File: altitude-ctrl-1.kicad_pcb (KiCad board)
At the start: 2 copper layers, 0 parts

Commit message: pcb: import components from schem
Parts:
- added C1: 10u, Capacitor_SMD:C_0805_2012Metric, F.Cu at (71.1, 154.0)
- added C10: 22u, Capacitor_SMD:C_0805_2012Metric, F.Cu at (80.0, 157.0)
- added C11: 0u1, Capacitor_SMD:C_0402_1005Metric, F.Cu at (83.2, 180.4)
- added C12: 10u, Capacitor_SMD:C_0805_2012Metric, F.Cu at (80.0, 160.0)
- added C13: 0u1, Capacitor_SMD:C_0402_1005Metric, F.Cu at (83.2, 182.3)
- added C14: 20p, Capacitor_SMD:C_0603_1608Metric, F.Cu at (89.5, 176.7)
- added C15: 20p, Capacitor_SMD:C_0603_1608Metric, F.Cu at (89.5, 179.2)
- added C16: 0u1, Capacitor_SMD:C_0402_1005Metric, F.Cu at (83.2, 184.3)
- added C17: 0u1, Capacitor_SMD:C_0402_1005Metric, F.Cu at (83.2, 186.3)
- added C18: 0u1, Capacitor_SMD:C_0402_1005Metric, F.Cu at (86.1, 176.4)
- added C19: 0u1, Capacitor_SMD:C_0402_1005Metric, F.Cu at (86.1, 178.4)
- added C2: 1u, Capacitor_SMD:C_0402_1005Metric, F.Cu at (83.2, 176.4)
- added C20: 1u, Capacitor_SMD:C_0402_1005Metric, F.Cu at (86.1, 180.4)
- added C21: 1u, Capacitor_SMD:C_0402_1005Metric, F.Cu at (86.1, 182.3)
- added C22: 0u1, Capacitor_SMD:C_0402_1005Metric, F.Cu at (86.1, 184.3)
- added C3: 1u, Capacitor_SMD:C_0402_1005Metric, F.Cu at (83.2, 178.4)
- added C4: 10u, Capacitor_SMD:C_0805_2012Metric, F.Cu at (71.1, 157.0)
- added C5: 22u, Capacitor_SMD:C_0805_2012Metric, F.Cu at (71.1, 160.0)
- added C6: 22u, Capacitor_SMD:C_0805_2012Metric, F.Cu at (75.6, 154.0)
- added C7: 22u, Capacitor_SMD:C_0805_2012Metric, F.Cu at (75.6, 157.0)
- added C8: 22u, Capacitor_SMD:C_0805_2012Metric, F.Cu at (75.6, 160.0)
- added C9: 22u, Capacitor_SMD:C_0805_2012Metric, F.Cu at (80.0, 154.0)
- added D1: SMAJ12A, Diode_SMD:D_SMA, F.Cu at (61.6, 179.3)
- added D10: YELLOW, LED_SMD:LED_0805_2012Metric, F.Cu at (68.3, 185.1)
- added D11: H5VU10U, GLCS:Diode_DFN1006, F.Cu at (86.2, 164.8)
- added D12: H5VU10U, GLCS:Diode_DFN1006, F.Cu at (86.2, 166.8)
- added D13: H5VU10U, GLCS:Diode_DFN1006, F.Cu at (86.2, 168.8)
- added D14: H5VU10U, GLCS:Diode_DFN1006, F.Cu at (86.2, 170.8)
- added D15: H5VU10U, GLCS:Diode_DFN1006, F.Cu at (86.2, 172.8)
- added D16: H5VU10U, GLCS:Diode_DFN1006, F.Cu at (89.3, 164.8)
- added D17: H5VU10U, GLCS:Diode_DFN1006, F.Cu at (89.3, 166.8)
- added D18: H5VU10U, GLCS:Diode_DFN1006, F.Cu at (89.3, 168.8)
- added D2: SMAJ12A, Diode_SMD:D_SMA, F.Cu at (61.6, 183.8)
- added D3: GREEN, LED_SMD:LED_0805_2012Metric, F.Cu at (68.3, 179.0)
- added D4: GREEN, LED_SMD:LED_0805_2012Metric, F.Cu at (68.3, 182.0)
- added D5: H5VU10U, GLCS:Diode_DFN1006, F.Cu at (83.2, 164.8)
- added D6: H5VU10U, GLCS:Diode_DFN1006, F.Cu at (83.2, 166.8)
- added D7: H5VU10U, GLCS:Diode_DFN1006, F.Cu at (83.2, 168.8)
- added D8: H5VU10U, GLCS:Diode_DFN1006, F.Cu at (83.2, 170.8)
- added D9: H5VU10U, GLCS:Diode_DFN1006, F.Cu at (83.2, 172.8)
- added FB1: 600Ω@100M, Inductor_SMD:L_0805_2012Metric, F.Cu at (85.8, 150.4)
- added FID1: Fiducial, Fiducial:Fiducial_1mm_Mask2mm, F.Cu at (54.5, 169.8)
- added FID2: Fiducial, Fiducial:Fiducial_1mm_Mask2mm, F.Cu at (54.5, 173.4)
- added FID3: Fiducial, Fiducial:Fiducial_1mm_Mask2mm, F.Cu at (54.5, 176.9)
- added H1: MountingHole, MountingHole:ToolingHole_1.152mm, F.Cu at (88.8, 131.7)
- added H2: MountingHole, MountingHole:ToolingHole_1.152mm, F.Cu at (88.8, 134.2)
- added H3: MountingHole, MountingHole:ToolingHole_1.152mm, F.Cu at (88.8, 136.6)
- added H4: MountingHole_Pad, MountingHole:MountingHole_3.2mm_M3_Pad_Via, F.Cu at (79.5, 120.1)
- added H5: MountingHole_Pad, MountingHole:MountingHole_3.2mm_M3_Pad_Via, F.Cu at (79.5, 128.0)
- added H6: MountingHole_Pad, MountingHole:MountingHole_3.2mm_M3_Pad_Via, F.Cu at (79.5, 136.0)
- added H7: MountingHole_Pad, MountingHole:MountingHole_3.2mm_M3_Pad_Via, F.Cu at (79.5, 143.9)
- added J1: Conn_01x02, TerminalBlock_Phoenix:TerminalBlock_Phoenix_MKDS-1,5-2-5.08_1x02_P5.08mm_Horizontal, F.Cu at (39.5, 122.3)
- added J10: Conn_01x02, Connector_JST:JST_XH_B2B-XH-A_1x02_P2.50mm_Vertical, F.Cu at (51.6, 163.6)
- added J2: Conn_01x02, TerminalBlock_Phoenix:TerminalBlock_Phoenix_MKDS-1,5-2-5.08_1x02_P5.08mm_Horizontal, F.Cu at (39.5, 134.5)
- added J3: Conn_01x05, TerminalBlock_Phoenix:TerminalBlock_Phoenix_MKDS-1,5-5-5.08_1x05_P5.08mm_Horizontal, F.Cu at (51.7, 122.3)
- added J4: TC2030, Connector:Tag-Connect_TC2030-IDC-NL_2x03_P1.27mm_Vertical, F.Cu at (52.1, 182.8)
- added J5: Conn_01x04_Pin, Connector_PinHeader_2.54mm:PinHeader_1x04_P2.54mm_Vertical, F.Cu at (50.4, 170.4)
- added J6: Conn_01x02, TerminalBlock_Phoenix:TerminalBlock_Phoenix_MKDS-1,5-2-5.08_1x02_P5.08mm_Horizontal, F.Cu at (39.5, 146.6)
- added J7: Conn_01x05, TerminalBlock_Phoenix:TerminalBlock_Phoenix_MKDS-1,5-5-5.08_1x05_P5.08mm_Horizontal, F.Cu at (51.7, 134.5)
- added J8: Conn_01x05, TerminalBlock_Phoenix:TerminalBlock_Phoenix_MKDS-1,5-5-5.08_1x05_P5.08mm_Horizontal, F.Cu at (51.7, 146.6)
- added J9: Conn_01x02, Connector_JST:JST_XH_B2B-XH-A_1x02_P2.50mm_Vertical, F.Cu at (51.6, 155.8)
- added JP1: Jumper_2_Small_Bridged, Connector_PinHeader_2.54mm:PinHeader_1x02_P2.54mm_Vertical, F.Cu at (85.8, 140.9)
- added R1: 10k, Resistor_SMD:R_0402_1005Metric, F.Cu at (74.5, 176.4)
- added R10: 10k, Resistor_SMD:R_0402_1005Metric, F.Cu at (77.4, 184.4)
- added R11: 10k, Resistor_SMD:R_0402_1005Metric, F.Cu at (80.3, 176.4)
- added R12: 560, Resistor_SMD:R_0603_1608Metric, F.Cu at (89.5, 181.7)
- added R13: 5k1, Resistor_SMD:R_0402_1005Metric, F.Cu at (80.3, 178.4)
- added R14: 100, Resistor_SMD:R_0402_1005Metric, F.Cu at (80.3, 180.4)
- added R15: 120, Resistor_SMD:R_1206_3216Metric, F.Cu at (86.3, 147.4)
- added R2: 1k, Resistor_SMD:R_0402_1005Metric, F.Cu at (74.5, 178.4)
- added R3: 1k, Resistor_SMD:R_0402_1005Metric, F.Cu at (74.5, 180.4)
- added R4: 5k1, Resistor_SMD:R_0402_1005Metric, F.Cu at (74.5, 182.4)
- added R5: 5k1, Resistor_SMD:R_0402_1005Metric, F.Cu at (74.5, 184.4)
- added R6: 5k1, Resistor_SMD:R_0402_1005Metric, F.Cu at (77.4, 176.4)
- added R7: 1k, Resistor_SMD:R_0402_1005Metric, F.Cu at (77.4, 178.4)
- added R8: 5k1, Resistor_SMD:R_0402_1005Metric, F.Cu at (77.4, 180.4)
- added R9: 10k, Resistor_SMD:R_0402_1005Metric, F.Cu at (77.4, 182.4)
- added SW1: SW_Push, Button_Switch_SMD:SW_SPST_TS-1088-xR020, F.Cu at (69.5, 166.1)
- added SW2: SW_SPST, TerminalBlock_Phoenix:TerminalBlock_Phoenix_MKDS-1,5-2-5.08_1x02_P5.08mm_Horizontal, F.Cu at (39.5, 158.7)
- added SW3: SW_Push, Button_Switch_SMD:SW_SPST_TS-1088-xR020, F.Cu at (69.5, 170.6)
- added SW4: SW_SPST, TerminalBlock_Phoenix:TerminalBlock_Phoenix_MKDS-1,5-2-5.08_1x02_P5.08mm_Horizontal, F.Cu at (39.5, 170.8)
- added SW5: SW_Push, Button_Switch_SMD:SW_SPST_TS-1088-xR020, F.Cu at (69.5, 175.2)
- added TC1: Thermocouple_Block, TerminalBlock_Phoenix:TerminalBlock_Phoenix_MKDS-1,5-2-5.08_1x02_P5.08mm_Horizontal, F.Cu at (39.5, 183.0)
- added TP1: TestPoint, TestPoint:TestPoint_Pad_D2.0mm, F.Cu at (85.5, 132.5)
- added TP2: TestPoint, TestPoint:TestPoint_Pad_D2.0mm, F.Cu at (85.5, 136.6)
- added U1: HT753-1, Package_TO_SOT_SMD:SOT-89-3, F.Cu at (86.9, 127.5)
- added U2: ULN2003A, Package_SO:SOIC-16_3.9x9.9mm_P1.27mm, F.Cu at (77.3, 169.7)
- added U3: LM73100, GLCS:Texas_RPW0010A_VQFN-HR-10_2x2mm_P0.5mm, F.Cu at (85.6, 118.2)
- added U4: LM73100, GLCS:Texas_RPW0010A_VQFN-HR-10_2x2mm_P0.5mm, F.Cu at (85.6, 122.3)
- added U5: MAX6675, Package_SO:SOIC-8_3.9x4.9mm_P1.27mm, F.Cu at (61.8, 167.2)
- added U6: STM32F103C8Tx, Package_QFP:LQFP-48_7x7mm_P0.5mm, F.Cu at (63.2, 158.1)
- added U7: SN65HVD230, Package_SO:SOIC-8_3.9x4.9mm_P1.27mm, F.Cu at (61.8, 173.8)
- added Y1: 8M, Crystal:Crystal_SMD_5032-2Pin_5.0x3.2mm, F.Cu at (85.9, 155.1)

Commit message: pcb: add initial sectioning
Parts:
- moved J6 220.7 mm to (260.1, 154.0), turned to 180 degrees
- moved J7 215.5 mm to (266.3, 115.2), turned to 180 degrees
- moved TC1 205.6 mm to (243.1, 154.4), turned to 180 degrees
- moved D15 194.4 mm to (268.2, 104.4), turned to 180 degrees
- moved D13 192.4 mm to (268.2, 106.4), turned to 180 degrees
- moved D11 190.5 mm to (268.2, 108.4), turned to 180 degrees
- moved D17 190.2 mm to (268.2, 102.4), turned to 180 degrees
- moved J2 187.1 mm to (225.7, 153.0), turned to 180 degrees
- moved R14 184.9 mm to (262.2, 147.1), turned to 180 degrees
- moved J8 182.1 mm to (231.1, 115.5), turned to 180 degrees
- moved U5 181.9 mm to (242.4, 145.1), turned to 180 degrees
- moved D2 168.1 mm to (225.2, 144.8), turned to 180 degrees
- moved SW4 165.2 mm to (196.2, 118.5), turned to 90 degrees
- moved J1 164.6 mm to (201.2, 152.7), turned to 180 degrees
- moved D14 160.2 mm to (233.0, 106.6), turned to 180 degrees
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
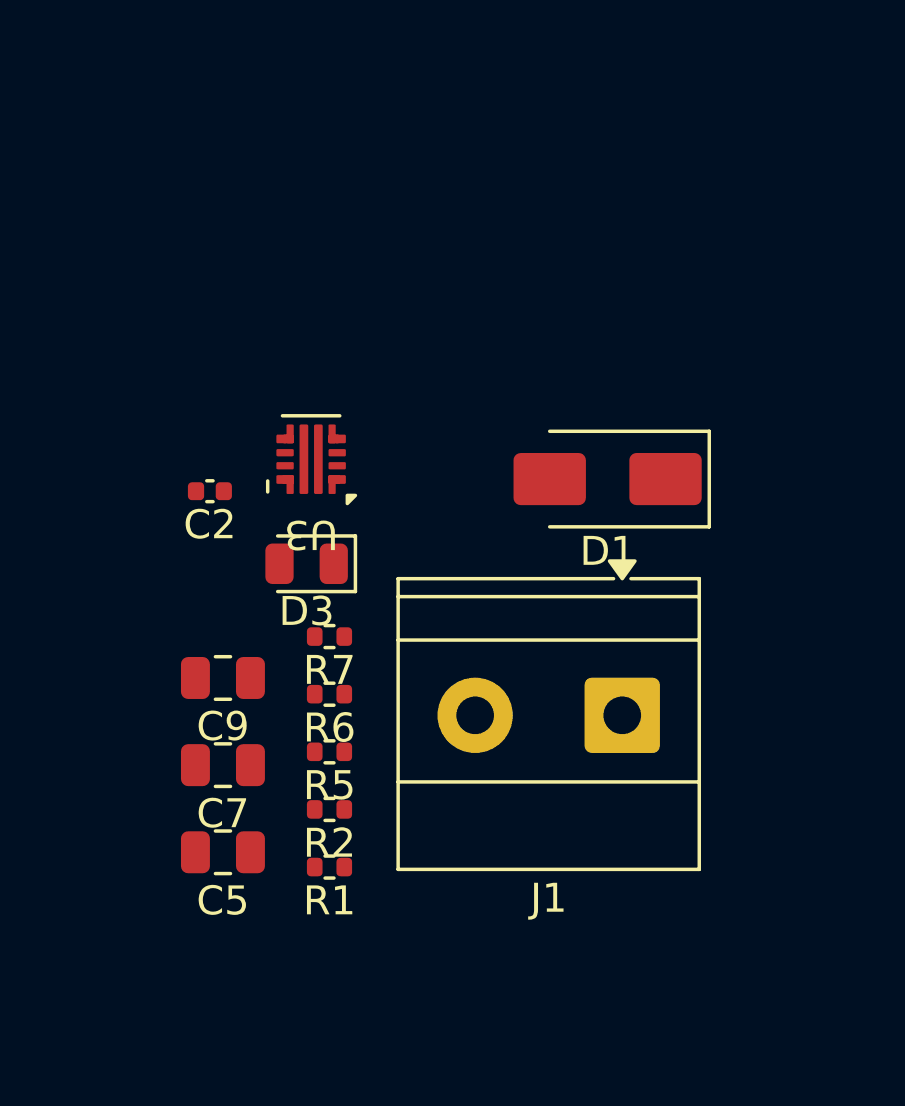
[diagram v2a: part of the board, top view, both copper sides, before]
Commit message: pcb: add +12v input protection layout
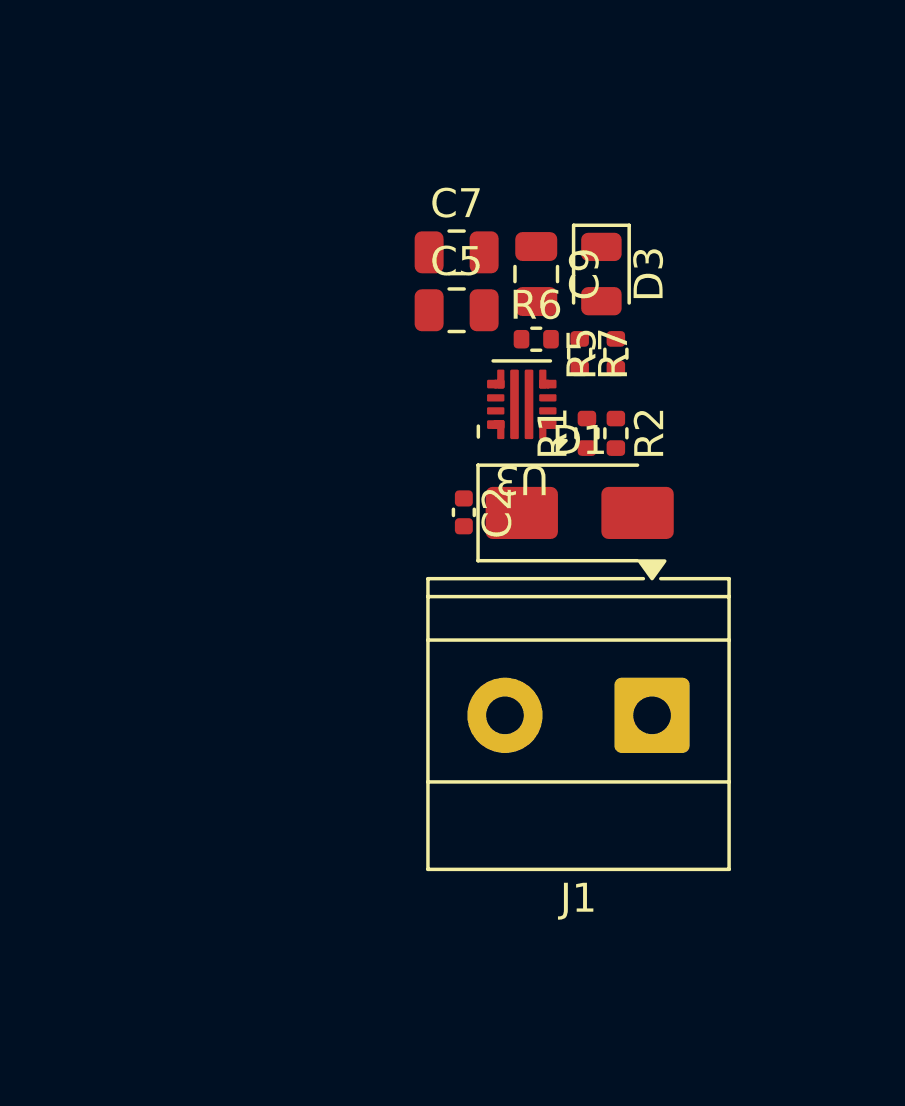
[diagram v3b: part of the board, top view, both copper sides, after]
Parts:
- moved C5 20.4 mm to (195.5, 138.8), turned to 0 degrees
- moved C7 19.5 mm to (195.5, 136.8), turned to 0 degrees
- moved C9 17.7 mm to (198.2, 137.5), turned to -90 degrees
- moved R1 17.4 mm to (200.0, 143.0), turned to 90 degrees
- moved R5 16.9 mm to (201.0, 140.2), turned to 90 degrees
- moved R2 16.3 mm to (201.0, 143.0), turned to -90 degrees
- moved D3 14.3 mm to (200.5, 137.5), turned to -90 degrees
- moved R6 14.2 mm to (198.2, 139.8), turned to 0 degrees
- moved R7 13.0 mm to (199.8, 140.2), turned to -90 degrees
- moved C2 8.80 mm to (195.8, 145.7), turned to -90 degrees
- moved U3 7.52 mm to (197.8, 142.0)
- moved D1 1.52 mm to (199.8, 145.8), turned to 0 degrees
- moved J1 1.03 mm to (202.2, 152.7)

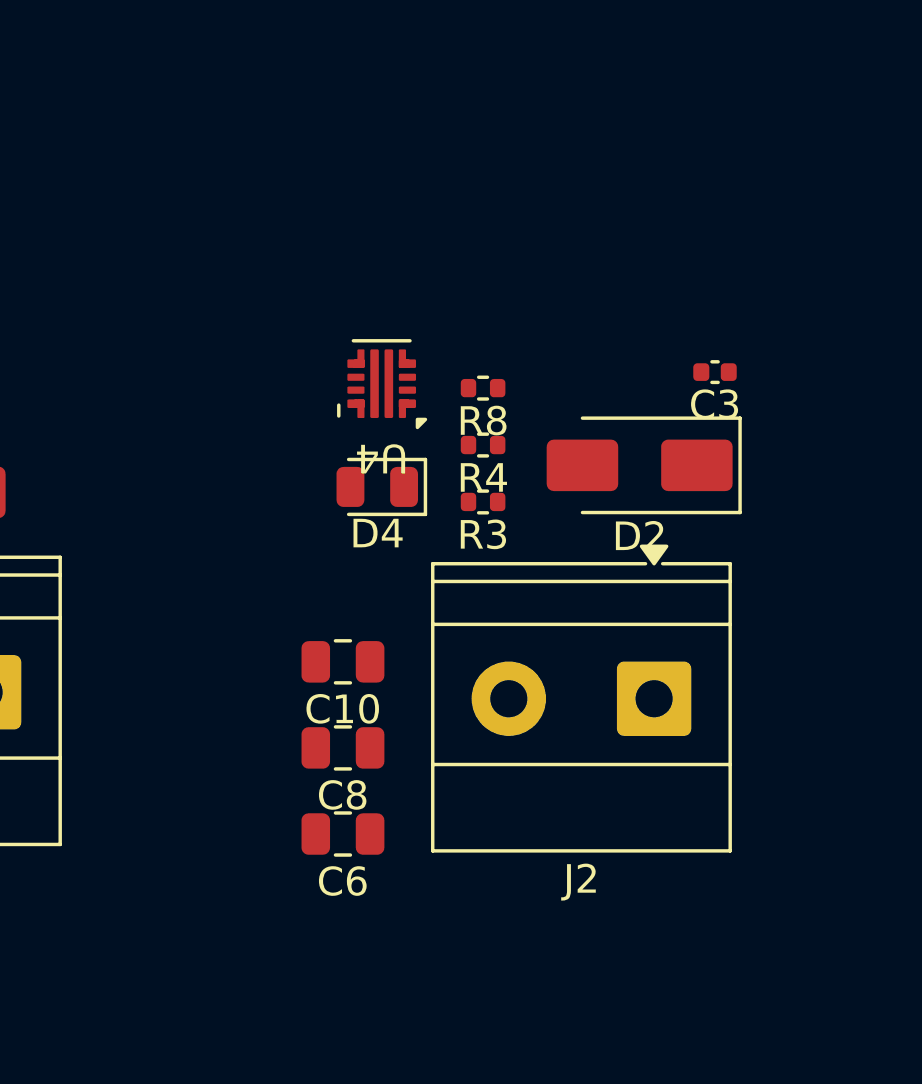
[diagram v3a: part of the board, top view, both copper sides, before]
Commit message: pcb: add +5v input protection layout
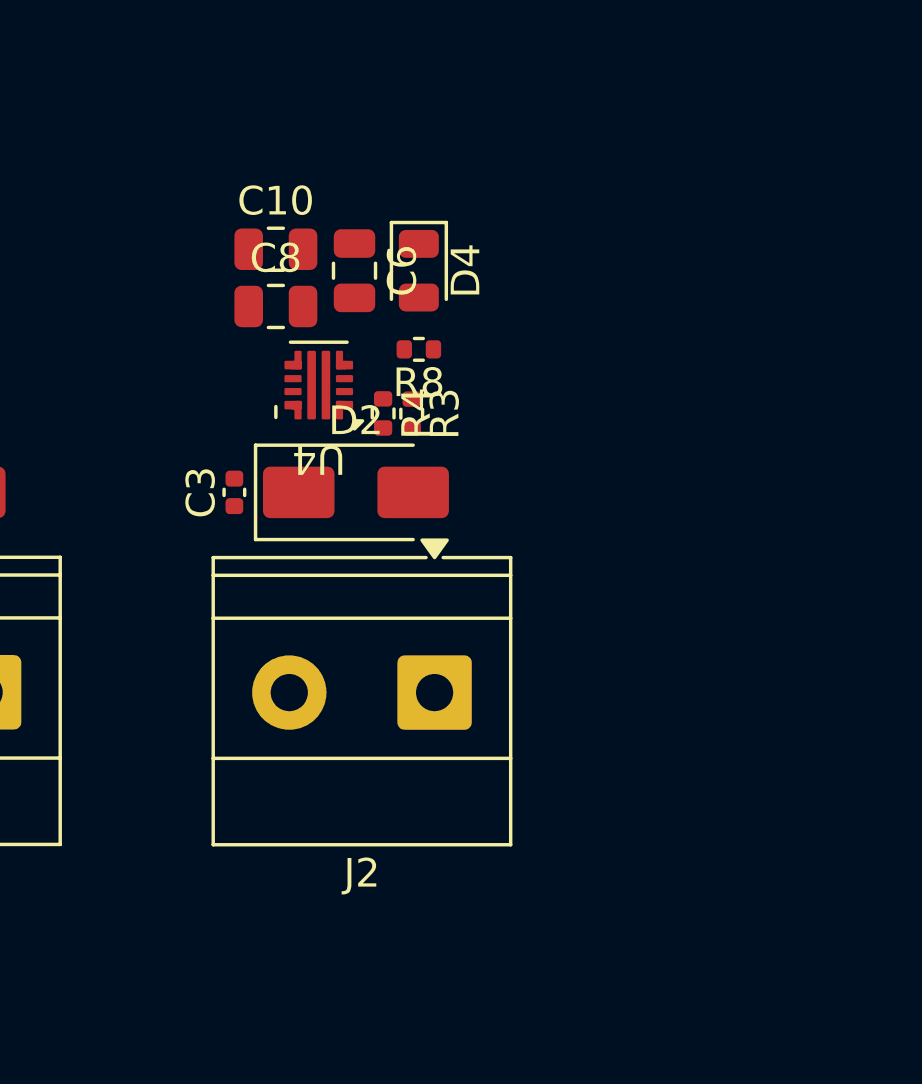
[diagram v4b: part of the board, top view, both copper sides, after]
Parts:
- moved C6 19.7 mm to (215.2, 138.0), turned to -90 degrees
- moved C3 17.3 mm to (211.0, 145.8), turned to 90 degrees
- moved C8 15.6 mm to (212.4, 139.2), turned to 0 degrees
- moved C10 14.6 mm to (212.4, 137.2), turned to 0 degrees
- moved D2 9.96 mm to (215.2, 145.8), turned to 0 degrees
- moved D4 7.70 mm to (217.4, 138.0), turned to -90 degrees
- moved J2 7.68 mm to (218.0, 152.8)
- moved R3 3.97 mm to (217.2, 143.0), turned to -90 degrees
- moved R4 3.67 mm to (216.2, 143.0), turned to -90 degrees
- moved R8 2.62 mm to (217.4, 140.8)
- moved U4 2.20 mm to (213.9, 142.0)

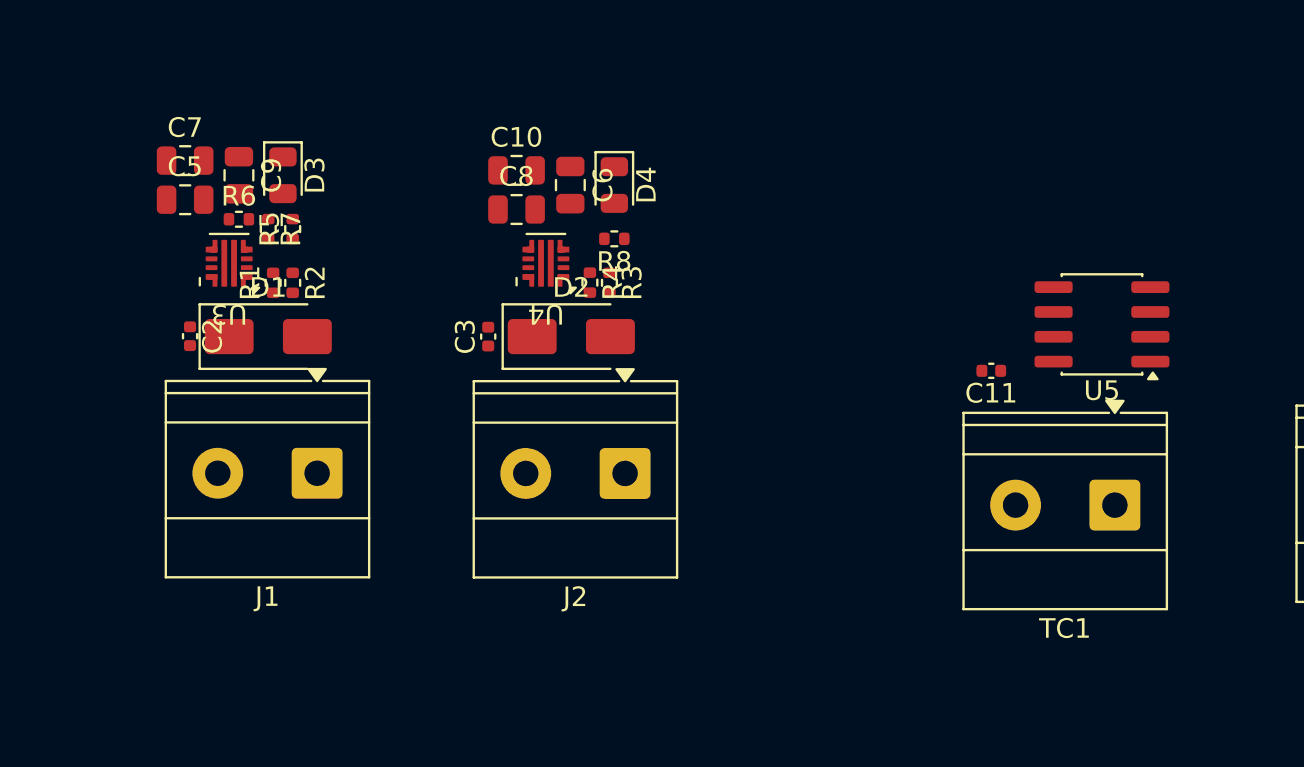
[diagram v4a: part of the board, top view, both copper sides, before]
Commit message: pcb: add thermocouple layout
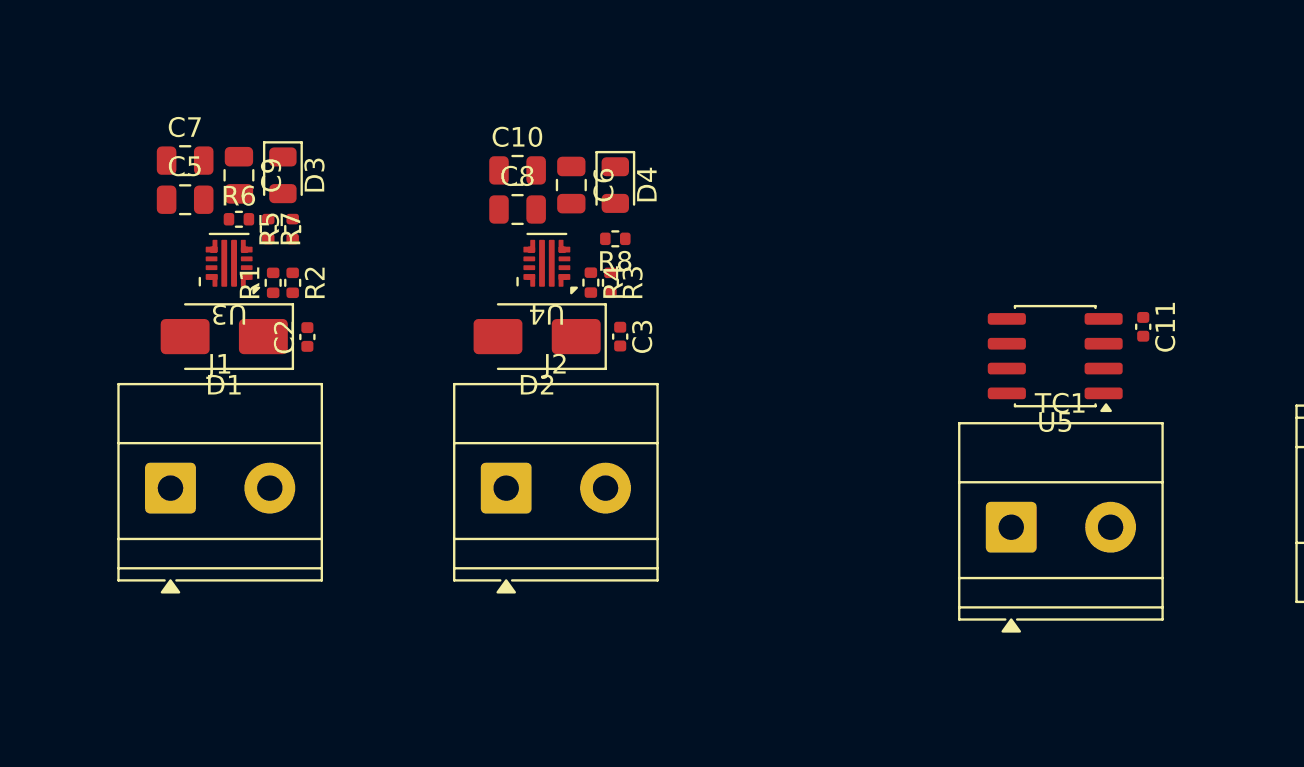
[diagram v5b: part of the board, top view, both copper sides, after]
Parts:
- moved C11 8.09 mm to (244.5, 145.2), turned to -90 degrees
- moved J1 7.54 mm to (194.8, 153.5), turned to 0 degrees
- moved C3 6.75 mm to (217.8, 145.8), turned to -90 degrees
- moved J2 6.13 mm to (211.9, 153.5), turned to 0 degrees
- moved C2 6.00 mm to (201.8, 145.8), turned to 90 degrees
- moved TC1 5.42 mm to (237.8, 155.5), turned to 0 degrees
- moved U5 2.89 mm to (240.0, 146.8)
- moved D1 2.25 mm to (197.5, 145.8), turned to 180 degrees
- moved D2 1.75 mm to (213.5, 145.8), turned to 180 degrees
- moved C10 0.05 mm to (212.5, 137.2)
- moved C6 0.05 mm to (215.2, 138.0)
- moved C8 0.05 mm to (212.5, 139.2)
- moved D4 0.05 mm to (217.5, 138.0)
- moved R3 0.05 mm to (217.2, 143.0)
- moved R4 0.05 mm to (216.2, 143.0)
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
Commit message: pcb: add can layout
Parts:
- moved C22 33.0 mm to (100.5, 177.3), turned to 90 degrees
- moved U7 27.8 mm to (105.0, 177.2)
- moved JP1 23.7 mm to (106.8, 182.5)
- moved R15 23.3 mm to (107.0, 188.2), turned to 180 degrees
- moved D12 15.7 mm to (217.3, 109.0), turned to 90 degrees
- moved D14 13.9 mm to (219.3, 109.0), turned to 90 degrees
- moved D11 13.5 mm to (254.8, 108.6), turned to 90 degrees
- moved D16 12.5 mm to (221.2, 109.0), turned to 90 degrees
- moved D13 11.7 mm to (256.8, 108.6), turned to 90 degrees
- moved D18 11.6 mm to (223.2, 109.0), turned to 90 degrees
- moved C1 10.4 mm to (157.5, 177.5), turned to -90 degrees
- moved D15 10.4 mm to (258.7, 108.6), turned to 90 degrees
- moved D17 9.71 mm to (260.7, 108.6), turned to 90 degrees
- moved J9 9.01 mm to (112.5, 178.2)
- moved J10 9.00 mm to (112.5, 185.5)
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
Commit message: pcb: add relay layout
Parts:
- moved J3 19.3 mm to (149.2, 154.8), turned to 0 degrees
- moved U2 9.20 mm to (159.0, 144.5), turned to -90 degrees
- moved TP1 4.84 mm to (166.2, 144.5)
